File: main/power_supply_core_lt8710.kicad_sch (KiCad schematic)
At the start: 33 parts, among them Q501 IXTP28P065T, Q502 TK4R3E06PL, U501 LT8710

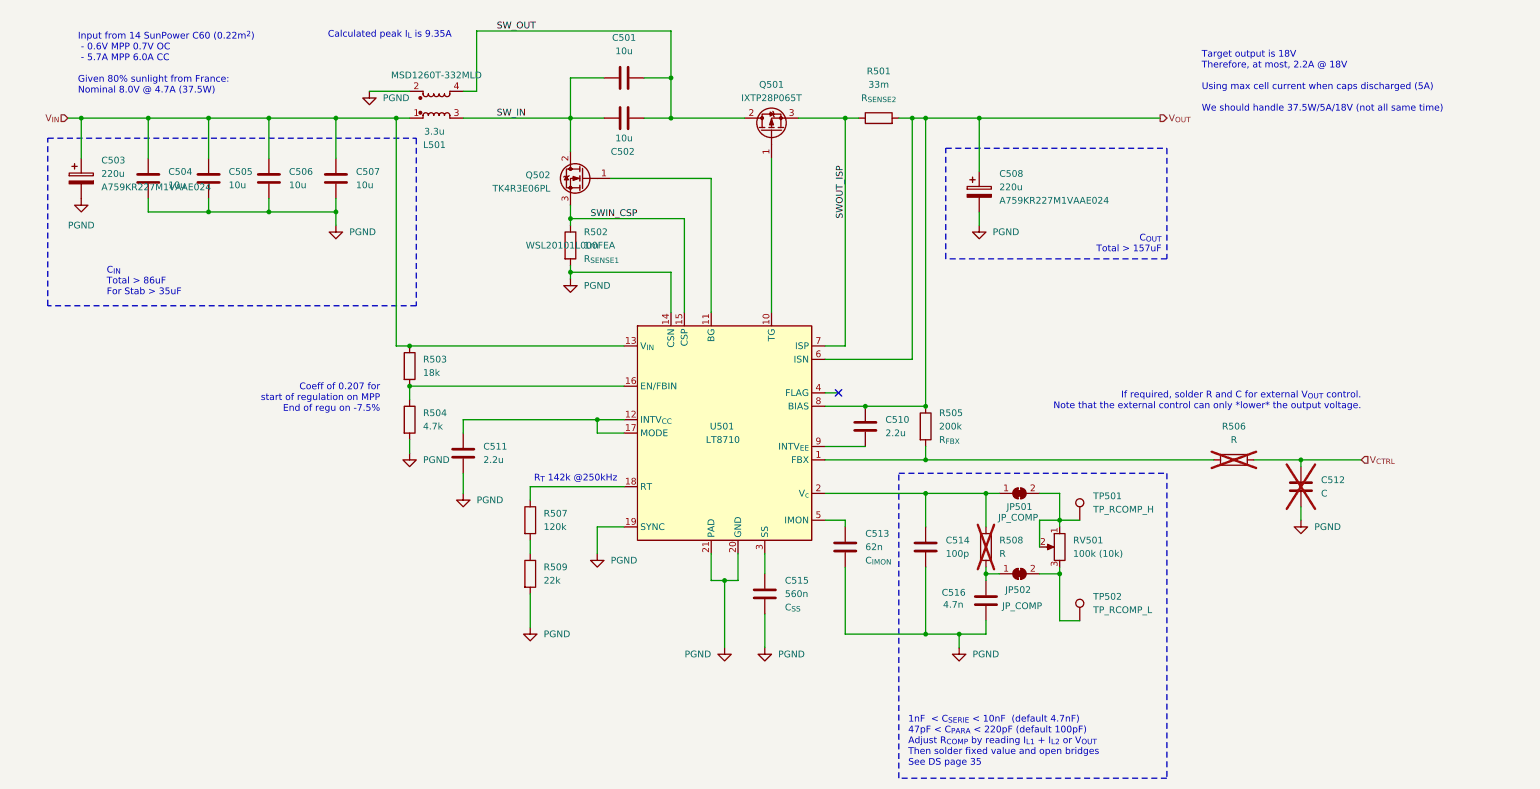
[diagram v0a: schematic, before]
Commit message: Clean silkscreen
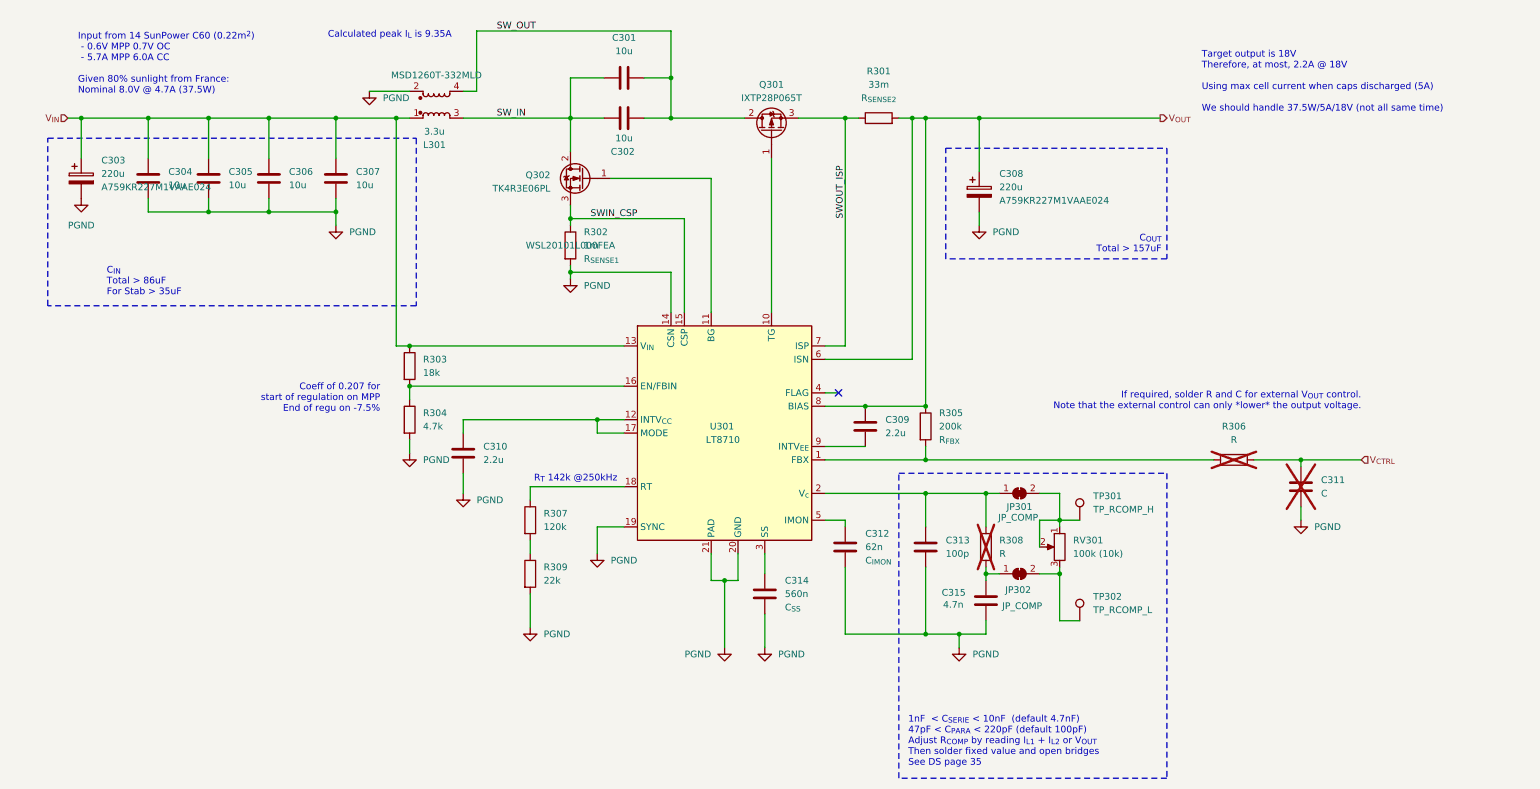
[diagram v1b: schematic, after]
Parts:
- renumbered C501 to C301, C502 to C302, C503 to C303, C504 to C304, C505 to C305, C506 to C306, C507 to C307, C508 to C308, C510 to C309, C511 to C310, C512 to C311, C513 to C312, C514 to C313, C515 to C314, C516 to C315, JP501 to JP301, JP502 to JP302, L501 to L301, Q501 to Q301, Q502 to Q302, R501 to R301, R502 to R302, R503 to R303, R504 to R304, R505 to R305, R506 to R306, R507 to R307, R508 to R308, R509 to R309, RV501 to RV301, TP501 to TP301, TP502 to TP302, U501 to U301

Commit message: Sent to fab
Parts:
- C301, C302, C304, C305, C306, C307: MPN (none) -> CL21A106KBYQNNE; Mouser SKU (none) -> 187-CL21A106KBYQNNE
- C303, C308: Mouser SKU (none) -> 80-A759KR227M1VAAE24
- C309, C310: MPN (none) -> CL21B225KBYNNWE; Mouser SKU (none) -> 187-CL21B225KBYNNWE
- C312: value 62n -> 68n; MPN (none) -> CL21B683KBCWPNC; Mouser SKU (none) -> 187-CL21B683KBCWPNC
- C313: MPN (none) -> CL21C101JBANNND; Mouser SKU (none) -> 187-CL21C101JBANNND
- C314: value 560n -> 680n; MPN (none) -> CL21B684JOFNNNE; Mouser SKU (none) -> 187-CL21B684JOFNNNE
- C315: MPN (none) -> CL21C472JAFNNNE; Mouser SKU (none) -> 187-CL21C472JAFNNNE
- L301: Mouser SKU (none) -> 994-MSD1260T-332MLD
- R301: MPN (none) -> TLM2HDR033FTE; Mouser SKU (none) -> 279-TLM2HDR033FTE
- R302: MPN WSL20101L000FEA -> WSL20101L000FEA18; Mouser SKU (none) -> 71-WSL20101L000FEA18
